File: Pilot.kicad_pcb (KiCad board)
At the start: 4 copper layers, 204 x 158 mm, 113 parts, among them J1 Touchscreen, J10 Conn_01x02, J11 Conn_01x02, J12 Conn_01x02, J13 3.5'' LCD, J14 USB_B_Micro, J15 Conn_01x03, J16 Conn_01x03, J17 Conn_01x03, J18 Conn_01x03, J19 Conn_01x03, J2 Conn_01x02, J20 USB_B_Micro, J21 Conn_01x02, J3 Conn_01x02, J4 Conn_01x02, J5 Conn_01x02, J6 Conn_01x02, J7 Conn_01x02, J8 Conn_01x02, J9 Conn_01x02, SW1 SW_SPDT, SW2 SW_SPDT, SW3 SW_SPDT, SW4 SW_SPDT, U1 STM32F103CBT6, U2 W25X40CLSS, U3 AT24CS01-XHM, U4 USBLC6-2SC6, U5 STM32F103C8T6, U6 USBLC6-2SC6, U8 AMS1117-3.3, Y1 8MHz, Y2 8MHz

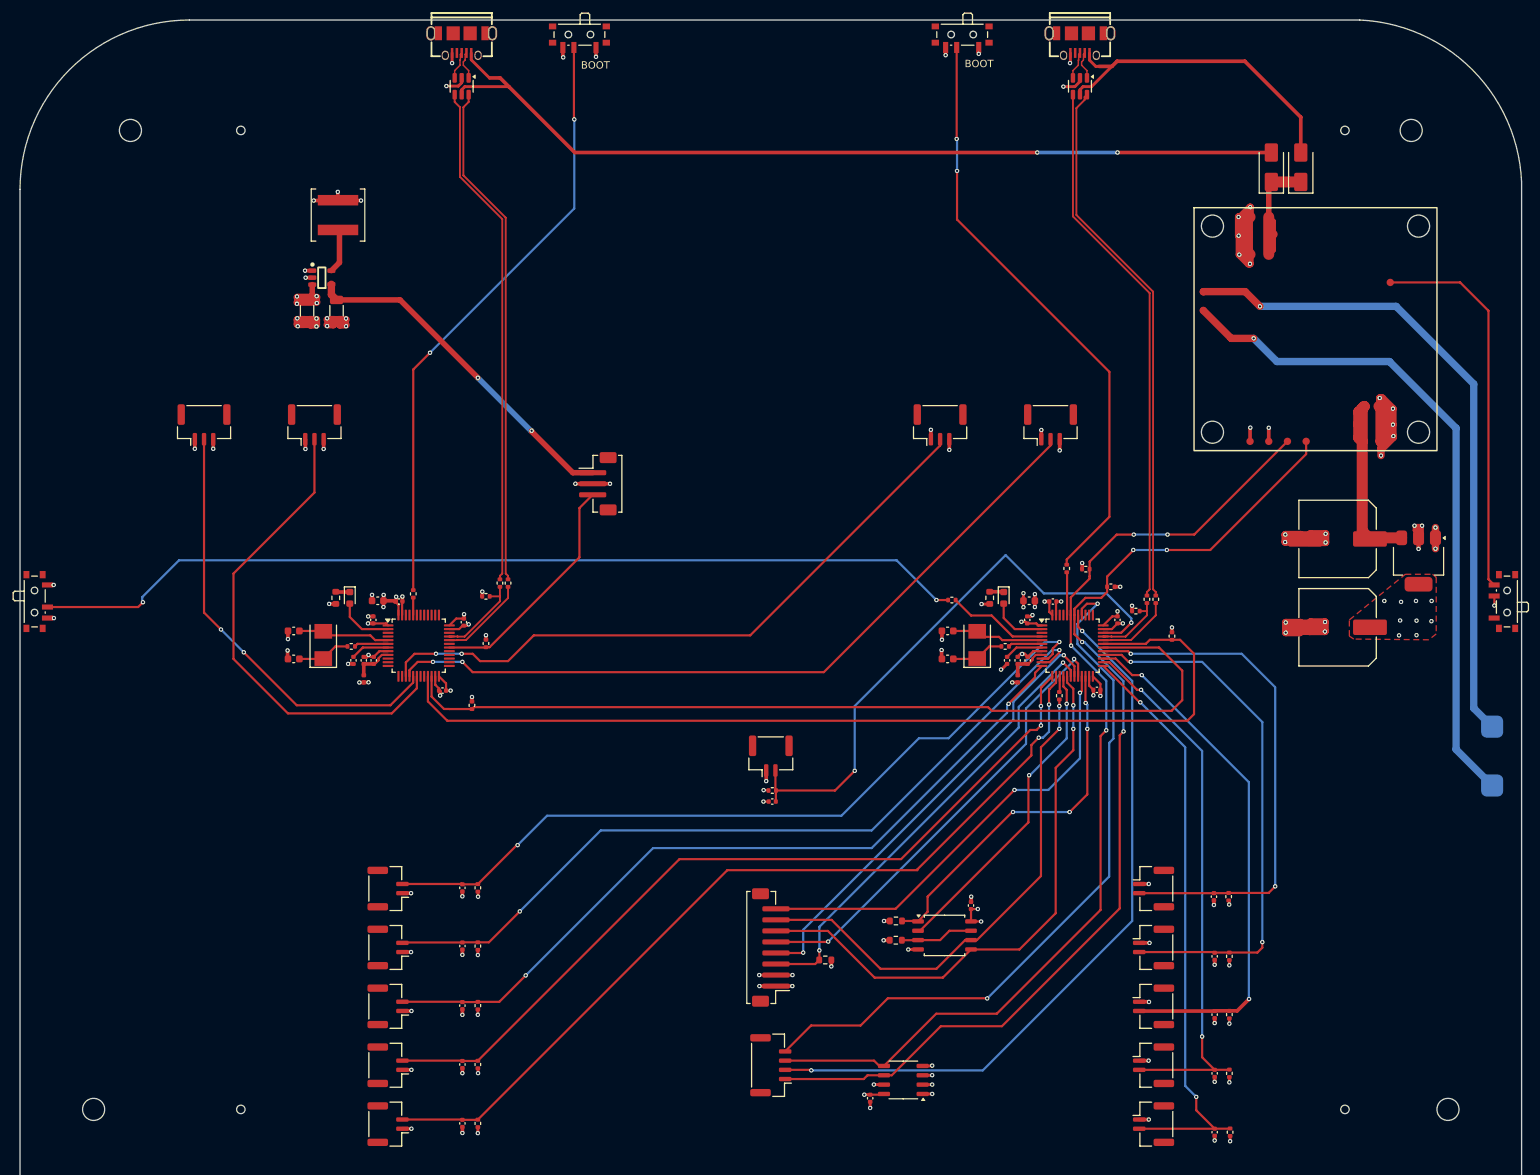
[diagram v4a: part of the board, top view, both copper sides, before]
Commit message: update to STM32F04
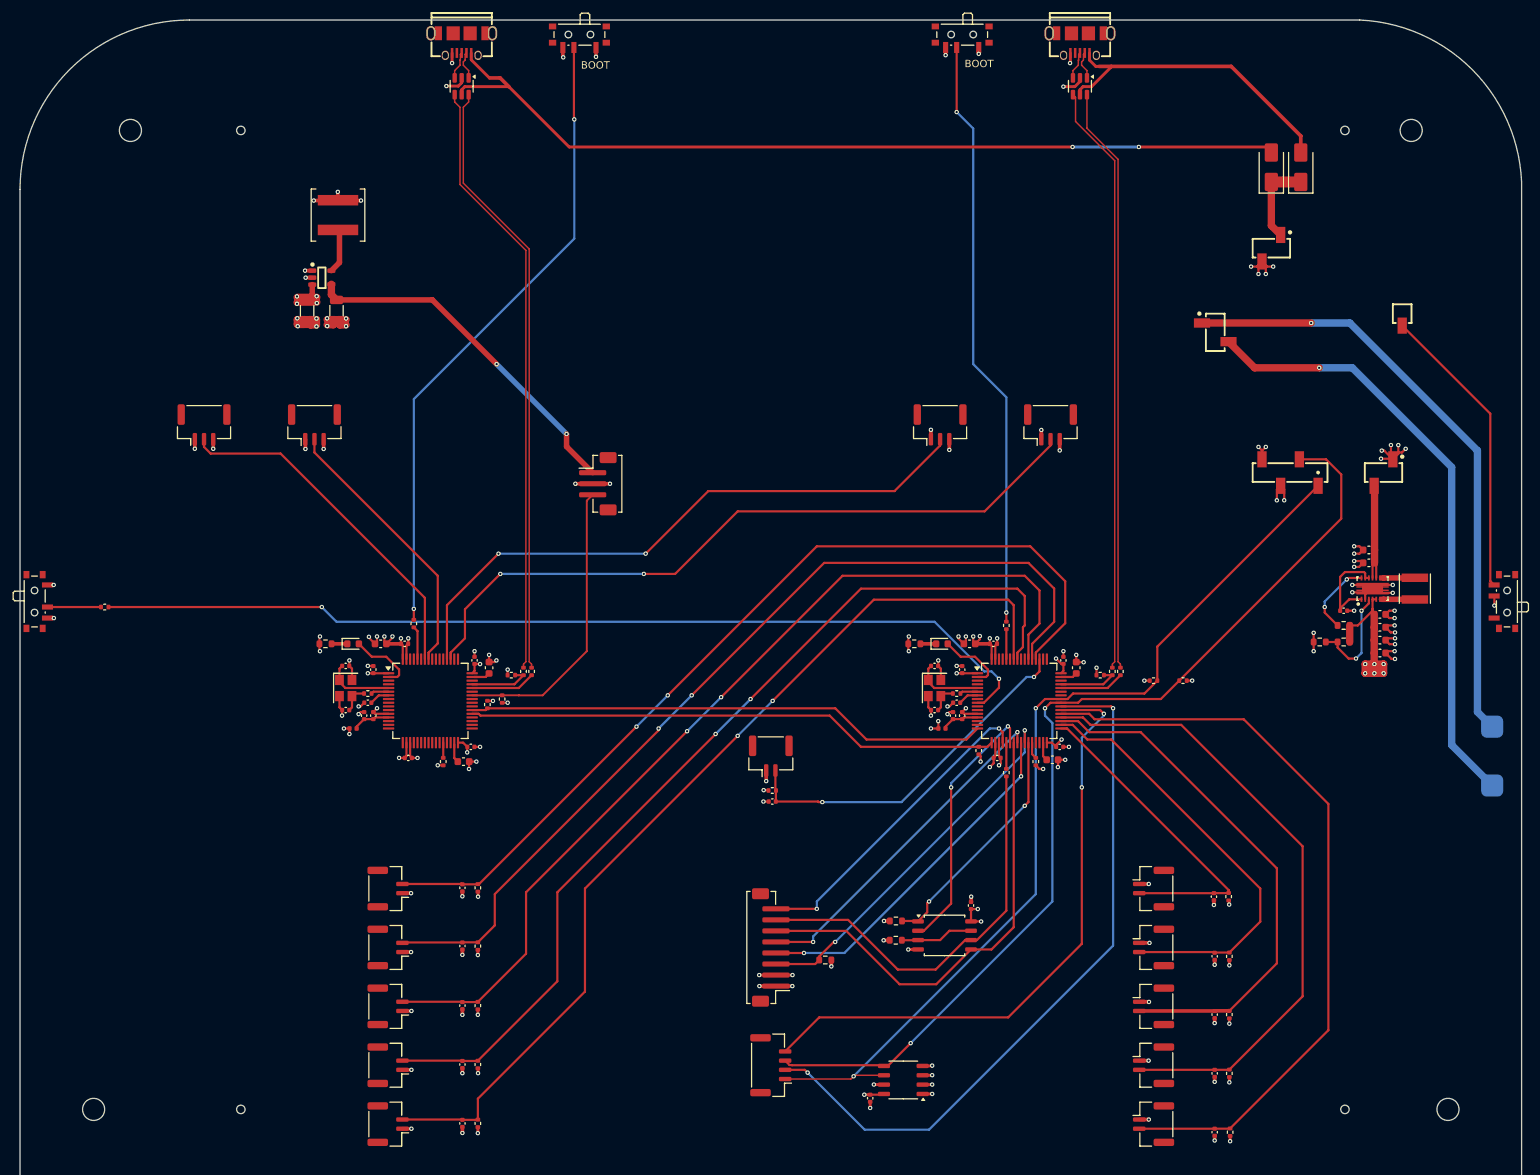
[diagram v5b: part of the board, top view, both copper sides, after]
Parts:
- removed the C24 at (45.3, 87.0)
- removed the C25 at (48.6, 78.9)
- removed the C26 at (48.0, 81.5)
- removed the R22 at (131.7, 78.5)
- removed the R26 at (156.5, 83.7)
- added C11: 10n, Capacitor_SMD:C_0402_1005Metric, F.Cu at (128.0, 94.5)
- added C12: 10p, Capacitor_SMD:C_0402_1005Metric, F.Cu at (124.2, 87.8)
- added C13: 10p, Capacitor_SMD:C_0402_1005Metric, F.Cu at (124.2, 93.8)
- added C36: 1u, Capacitor_SMD:C_0402_1005Metric, F.Cu at (46.8, 94.5)
- added C37: 10n, Capacitor_SMD:C_0402_1005Metric, F.Cu at (48.0, 94.5)
- added C38: 10p, Capacitor_SMD:C_0402_1005Metric, F.Cu at (44.2, 87.8)
- added C39: 10p, Capacitor_SMD:C_0402_1005Metric, F.Cu at (44.2, 93.8)
- added C42: 100n, Capacitor_SMD:C_0402_1005Metric, F.Cu at (179.8, 80.2)
- added C43: 10u, Capacitor_SMD:C_0603_1608Metric, F.Cu at (183.2, 73.8)
- added C44: 10u, Capacitor_SMD:C_0603_1608Metric, F.Cu at (183.2, 72.0)
- added C45: 22u, Capacitor_SMD:C_0603_1608Metric, F.Cu at (184.8, 80.8)
- added C46: 22u, Capacitor_SMD:C_0603_1608Metric, F.Cu at (184.8, 82.5)
- added C47: 22u, Capacitor_SMD:C_0603_1608Metric, F.Cu at (184.8, 84.2)
- added C48: 22u, Capacitor_SMD:C_0603_1608Metric, F.Cu at (184.8, 86.0)
- added L4: 1u5, Inductor_SMD:L_Vishay_IFSC-1515AH_4x4x1.8mm, F.Cu at (189.5, 77.2)
- added R12: 10k, Resistor_SMD:R_0402_1005Metric, F.Cu at (11.5, 79.8)
- added R24: 1k, Resistor_SMD:R_0603_1608Metric, F.Cu at (121.5, 84.8)
- added R34: 47, Resistor_SMD:R_0402_1005Metric, F.Cu at (47.2, 91.5)
- added R35: 1k, Resistor_SMD:R_0603_1608Metric, F.Cu at (41.5, 84.8)
- added R36: 180k, Resistor_SMD:R_0603_1608Metric, F.Cu at (176.6, 84.5)
- added R37: 1M, Resistor_SMD:R_0603_1608Metric, F.Cu at (179.8, 82.2)
- added R38: 1M, Resistor_SMD:R_0603_1608Metric, F.Cu at (179.8, 84.5)
- added U10: ~, kwrzesni:DZ254S-11-02-48, F.Cu at (185.2, 61.5)
- added U11: ~, kwrzesni:X6511WVS-04H-C60D48R1, F.Cu at (172.5, 61.5)
- added U13: ~, kwrzesni:TPS63020DSJR, F.Cu at (183.8, 77.2)
- added U9: ~, kwrzesni:DZ254S-11-02-48, F.Cu at (170.0, 31.0)
- C10: value 30p -> 1u; footprint Capacitor_SMD:C_0603_1608Metric -> Capacitor_SMD:C_0402_1005Metric
- C2: value 4u7 -> 2u2
- C28, C29, C3: value 100n -> 2u2; footprint Capacitor_SMD:C_0402_1005Metric -> Capacitor_SMD:C_0603_1608Metric
- C30: value 1u -> 4u7; footprint Capacitor_SMD:C_0402_1005Metric -> Capacitor_SMD:C_0603_1608Metric
- C31, C8: value 10n -> 100n
- C32, C33, C9: value 30p -> 100n; footprint Capacitor_SMD:C_0603_1608Metric -> Capacitor_SMD:C_0402_1005Metric
- C34, C35: value 10u -> 100n; footprint Capacitor_SMD:C_Elec_10x10.2 -> Capacitor_SMD:C_0402_1005Metric
- C4: value 100n -> 4u7; footprint Capacitor_SMD:C_0402_1005Metric -> Capacitor_SMD:C_0603_1608Metric
- C7: value 1u -> 100n
- R10: value 10k -> 47
- R2: value 2k2 -> 10k
- R28: value 22R -> 10k
- R31: value 10k -> 22R
- R32, R9: value 0 -> 10k
- R33: value 1k -> 10k; footprint Resistor_SMD:R_0603_1608Metric -> Resistor_SMD:R_0402_1005Metric
- R4: value 10k -> 2k2
- R5: value 22R -> 22R-
- R6: value 22R -> 1k5
- R7: value 1k5 -> 22R+
- U1: value STM32F103CBT6 -> STM32F405RGT6; footprint Package_QFP:LQFP-48_7x7mm_P0.5mm -> Package_QFP:LQFP-64_10x10mm_P0.5mm
- U5: value STM32F103C8T6 -> STM32F405RGT6; footprint Package_QFP:LQFP-48_7x7mm_P0.5mm -> Package_QFP:LQFP-64_10x10mm_P0.5mm
- U7: footprint kwrzesni:BatteryBabysitter -> kwrzesni:DZ254S-11-02-48
- U8: value AMS1117-3.3 -> ~; footprint Package_TO_SOT_SMD:SOT-223-3_TabPin2 -> kwrzesni:X6511WVS-01H-C60D48R2
- Y1, Y2: value 8MHz -> 16Mhz; footprint Crystal:Crystal_SMD_5032-2Pin_5.0x3.2mm -> Crystal:Crystal_SMD_3225-4Pin_3.2x2.5mm
- moved C35 126.8 mm to (52.2, 84.8), turned to 0 degrees
- moved C34 118.4 mm to (61.8, 87.0), turned to 90 degrees
- moved R4 92.7 mm to (154.0, 89.8), turned to 0 degrees
- moved R2 83.4 mm to (63.5, 93.0), turned to 90 degrees
- moved R27 68.5 mm to (130.2, 99.2), turned to -90 degrees
- moved U8 32.1 mm to (187.8, 41.5), turned to 0 degrees
- moved C33 26.9 mm to (61.2, 98.8)
- moved R8 26.6 mm to (138.0, 100.8), turned to 90 degrees
- moved C32 23.2 mm to (52.8, 100.2), turned to 180 degrees
- moved C6 22.6 mm to (132.8, 100.2), turned to 180 degrees
- moved C5 22.2 mm to (128.0, 88.2), turned to 90 degrees
- moved C2 21.8 mm to (140.2, 100.5), turned to 0 degrees
- moved R32 20.0 mm to (57.5, 100.8), turned to 90 degrees
- moved C28 19.0 mm to (60.2, 100.8), turned to 0 degrees
- moved C4 18.4 mm to (129.0, 84.8)
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- renumbered C11 to C14, C12 to C15, C13 to C16, C14 to C17, C15 to C18, C16 to C19, C17 to C20, C18 to C21, C19 to C22, C20 to C23, C21 to C24, C22 to C25, C23 to C26, C36 to C40, C37 to C41, R23 to R11, R11 to R13, R12 to R14, R13 to R15, R14 to R16, R15 to R17, R16 to R18, R17 to R19, R18 to R20, R19 to R21, R20 to R22, R21 to R23, R24 to R25, R25 to R26, U9 to U12
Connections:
- C10 pad 1: GND -> 3.3VA_1
- C10 pad 2: Net-(C10-Pad2) -> GND
- C2 pad 1: +3.3V -> Net-(U1-VCAP_1)
- C27 pad 1: +3.3V -> Net-(U5-NRST)
- C28 pad 1: +3.3V -> Net-(U5-VCAP_1)
- C29 pad 1: +3.3V -> Net-(U5-VCAP_2)
- C3 pad 1: +3.3V -> Net-(U1-VCAP_2)
- C30 pad 1: 3.3VA_2 -> +3.3V
- C31 pad 1: 3.3VA_2 -> +3.3V
- C32 pad 1: GND -> +3.3V
- C32 pad 2: HSE_IN_2 -> GND
- C33 pad 1: GND -> +3.3V
- C33 pad 2: Net-(C33-Pad2) -> GND
- C34 pad 1: Net-(U7-Vout+) -> +3.3V
- C7 pad 1: 3.3VA_1 -> +3.3V
- C8 pad 1: 3.3VA_1 -> +3.3V
- C9 pad 1: GND -> +3.3V
- C9 pad 2: HSE_IN_1 -> GND
- R1 pad 2: BATTERY_SCL -> BATTERY_SDA
- R10 pad 1: Net-(SW2-B) -> HSE_OUT_1
- R10 pad 2: LCD_SWITCH -> Net-(C13-Pad2)
- R2 pad 1: +3.3V -> USART2_TX1
- R2 pad 2: BATTERY_SDA -> +3.3V
- R27 pad 1: CRSF -> USART2_RX1
- R28 pad 1: USB2- -> CRSF
- R28 pad 2: Net-(U5-PA11) -> +3.3V
- R29 pad 1: USB2+ -> USB2-
- R29 pad 2: Net-(U5-PA12) -> Net-(U5-PA11)
- R31 pad 1: Net-(SW3-B) -> USB2+
- R31 pad 2: BOOT0_2 -> Net-(U5-PA12)
- R32 pad 1: HSE_OUT_2 -> GND
- R32 pad 2: Net-(C33-Pad2) -> Net-(U5-PB2)
- R33 pad 1: Net-(D2-K) -> Net-(SW3-B)
- R33 pad 2: GND -> BOOT0_2
- R4 pad 1: USART1_TX1 -> +3.3V
- R4 pad 2: +3.3V -> BATTERY_SCL
- R6 pad 1: USB1+ -> +3.3V
- R7 pad 1: +3.3V -> USB1+
- R8 pad 1: Net-(SW1-B) -> GND
- R8 pad 2: BOOT0_1 -> Net-(U1-PB2)
- R9 pad 1: HSE_OUT_1 -> Net-(SW1-B)
- R9 pad 2: Net-(C10-Pad2) -> BOOT0_1
- U1 pad 10: MENU_BUTTON -> unconnected-(U1-PC2-Pad10)
- U1 pad 11: HOME_BUTTON -> unconnected-(U1-PC3-Pad11)
- U1 pad 12: PAGE_UP_BUTTON -> GND
- U1 pad 13: PAGE_DOWN_BUTTON -> 3.3VA_1
- U1 pad 14: BACK_BUTTON -> unconnected-(U1-PA0-Pad14)
- U1 pad 15: Net-(U1-PA5) -> unconnected-(U1-PA1-Pad15)
- U1 pad 16: SPI1_MISO -> USART2_TX1
- U1 pad 17: SPI1_MOSI -> USART2_RX1
- U1 pad 18: LCD_CS -> GND
- U1 pad 19: LCD_RESET -> +3.3V
- U1 pad 20: LCD_DC -> LCD_LED
- U1 pad 21: LCD_LED -> Net-(U1-PA5)
- U1 pad 22: FLASH_CS -> SPI1_MISO
- U1 pad 23: GND -> SPI1_MOSI
- U1 pad 24: +3.3V -> LCD_DC
- U1 pad 25: DOWN_BUTTON -> LCD_RESET
- U1 pad 26: RIGHT_BUTTON -> LCD_CS
- U1 pad 27: OK_BUTTON -> FLASH_CS
- U1 pad 28: LEFT_BUTTON -> Net-(U1-PB2)
- U1 pad 29: UP_BUTTON -> unconnected-(U1-PB10-Pad29)
- U1 pad 30: USART1_TX1 -> unconnected-(U1-PB11-Pad30)
- U1 pad 31: USART1_RX1 -> Net-(U1-VCAP_1)
- U1 pad 32: Net-(U1-PA11) -> +3.3V
- U1 pad 33: Net-(U1-PA12) -> UP_BUTTON
- U1 pad 34: ON_BUTTON -> LEFT_BUTTON
- U1 pad 35: GND -> OK_BUTTON
- U1 pad 36: +3.3V -> RIGHT_BUTTON
- U1 pad 37: unconnected-(U1-PA14-Pad37) -> DOWN_BUTTON
- U1 pad 38: unconnected-(U1-PA15-Pad38) -> TOUCHSCREEN_INT
- U1 pad 39: unconnected-(U1-PB3-Pad39) -> TOUCHSCREEN_RESET
- U1 pad 4: LCD_SWITCH -> unconnected-(U1-PC15-Pad4)
- U1 pad 40: TOUCHSCREEN_INT -> BATTERY_SDA
- U1 pad 41: TOUCHSCREEN_RESET -> BATTERY_SCL
- U1 pad 42: BATTERY_SCL -> unconnected-(U1-PA9-Pad42)
- U1 pad 43: BATTERY_SDA -> unconnected-(U1-PA10-Pad43)
- U1 pad 44: BOOT0_1 -> Net-(U1-PA11)
- U1 pad 45: unconnected-(U1-PB8-Pad45) -> Net-(U1-PA12)
- U1 pad 47: GND -> Net-(U1-VCAP_2)
- U1 pad 8: GND -> unconnected-(U1-PC0-Pad8)
- U1 pad 9: 3.3VA_1 -> LCD_SWITCH
- U5 pad 12: unconnected-(U5-PA2-Pad12) -> GND
- U5 pad 13: unconnected-(U5-PA3-Pad13) -> 3.3VA_2
- U5 pad 15: RIGHT_GIMBAL_V -> unconnected-(U5-PA1-Pad15)
- U5 pad 16: RIGHT_GIMBAL_H -> unconnected-(U5-PA2-Pad16)
- U5 pad 17: LEFT_GIMBAL_V -> unconnected-(U5-PA3-Pad17)
- U5 pad 18: LEFT_GIMBAL_H -> GND
- U5 pad 19: unconnected-(U5-PB1-Pad19) -> +3.3V
- U5 pad 21: USART1_RX1 -> unconnected-(U5-PA5-Pad21)
- U5 pad 22: USART1_TX1 -> unconnected-(U5-PA6-Pad22)
- U5 pad 23: GND -> unconnected-(U5-PA7-Pad23)
- U5 pad 24: +3.3V -> unconnected-(U5-PC4-Pad24)
- U5 pad 28: unconnected-(U5-PB15-Pad28) -> Net-(U5-PB2)
- U5 pad 30: CRSF -> unconnected-(U5-PB11-Pad30)
- U5 pad 31: unconnected-(U5-PA10-Pad31) -> Net-(U5-VCAP_1)
- U5 pad 32: Net-(U5-PA11) -> +3.3V
- U5 pad 33: Net-(U5-PA12) -> unconnected-(U5-PB12-Pad33)
- U5 pad 35: GND -> unconnected-(U5-PB14-Pad35)
- U5 pad 36: +3.3V -> unconnected-(U5-PB15-Pad36)
- U5 pad 37: unconnected-(U5-PA14-Pad37) -> USART2_RX1
- U5 pad 38: unconnected-(U5-PA15-Pad38) -> USART2_TX1
- U5 pad 42: unconnected-(U5-PB6-Pad42) -> CRSF
- U5 pad 44: BOOT0_2 -> Net-(U5-PA11)
- U5 pad 45: unconnected-(U5-PB8-Pad45) -> Net-(U5-PA12)
- U5 pad 47: GND -> Net-(U5-VCAP_2)
- U5 pad 8: GND -> unconnected-(U5-PC0-Pad8)
- U5 pad 9: 3.3VA_2 -> unconnected-(U5-PC1-Pad9)
- U8 pad 1: GND -> Net-(SW4-C)
- Y1 pad 1: Net-(C10-Pad2) -> HSE_IN_1
- Y1 pad 2: HSE_IN_1 -> GND
- Y2 pad 1: Net-(C33-Pad2) -> HSE_IN_2
- Y2 pad 2: HSE_IN_2 -> GND
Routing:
- net USART1_RX1: track 130.5 -> 0.00 mm
- net USART1_TX1: track 122.4 -> 0.00 mm
- net Net-(SW2-B): track 128.1 -> 7.27 mm, vias 2 -> 0
- net LCD_SWITCH: track 13.8 -> 130.0 mm, vias 0 -> 2
- net USART2_RX1: track 0.00 -> 72.7 mm
- net USART2_TX1: track 0.00 -> 71.1 mm
- net +3.3V: track 108.8 -> 139.7 mm, vias 80 -> 78
- net ON_BUTTON: track 79.5 -> 49.2 mm
- net Net-(U7-Vout+): track 28.2 -> 0.00 mm
- net UP_BUTTON: track 71.3 -> 44.4 mm, vias 2 -> 0
- net LEFT_GIMBAL_V: track 59.3 -> 37.3 mm, vias 2 -> 0
- net DOWN_BUTTON: track 81.6 -> 103.4 mm, vias 2 -> 0
- net PAGE_UP_BUTTON: track 106.8 -> 126.2 mm
- net RIGHT_GIMBAL_H: track 102.6 -> 84.2 mm
- net LCD_LED: track 61.0 -> 43.2 mm
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- removed copper zone on F.Cu, net +3.3V
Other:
- outline, holes or cut-outs redrawn
